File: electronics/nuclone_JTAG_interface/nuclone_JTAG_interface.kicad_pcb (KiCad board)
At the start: 2 copper layers, 50 x 50 mm, 44 parts, among them J3 nuclone_small_left, J4 nuclone_small_right

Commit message: WIP schematic
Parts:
- added J1: DevBoardUartInput, Connector_JST:JST_PH_B4B-PH-K_1x04_P2.00mm_Vertical, F.Cu at (91.3, 63.9)
- added J2: JTAG_2X10_OUT, SquantorConnectors:Header-0254-2X10-H010, F.Cu at (85.0, 107.6)
- added J5: Conn_02x05_Odd_Even, SquantorConnectors:Header-0127-2X05-H006, F.Cu at (100.3, 103.1)
- added TP36: RX, SquantorTestPoints:TestPoint_hole_H05R10_2side, F.Cu at (95.3, 68.2)
- added TP37: TX, SquantorTestPoints:TestPoint_hole_H05R10_2side, F.Cu at (97.3, 68.2)
- N2: value V20220513 -> V20230220
- moved N1 10.9 mm to (84.8, 92.8)
- moved N2 10.9 mm to (84.9, 96.5)
- moved N3 10.9 mm to (84.8, 98.0)
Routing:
- net /VBUS: track 7.40 -> 47.1 mm
- net /target_RESET: track 0.00 -> 26.2 mm, vias 0 -> 1
- net /target_TDO: track 0.00 -> 23.1 mm, vias 0 -> 1
- net /target_TCK: track 0.00 -> 17.5 mm, vias 0 -> 1
- net /target_TMS: track 0.00 -> 14.4 mm, vias 0 -> 1
- net /target_TDI: track 0.00 -> 11.8 mm, vias 0 -> 1
- net Net-(J1-Pad4): track 0.00 -> 4.30 mm
- net Net-(J1-Pad3): track 0.00 -> 4.30 mm
- net /vtarget: track 0.00 -> 2.54 mm

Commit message: WIP schematic definition
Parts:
- added C1: 1uF, SquantorRcl:C_0402, F.Cu at (85.6, 77.9)
- added C2: 1uF, SquantorRcl:C_0402, F.Cu at (88.0, 82.0)
- added C3: 1uF, SquantorRcl:C_0402, F.Cu at (88.7, 85.0)
- added C4: 1uF, SquantorRcl:C_0402, F.Cu at (83.8, 81.0)
- added C5: 1uF, SquantorRcl:C_0402, F.Cu at (85.9, 81.0)
- added C6: 1uF, SquantorRcl:C_0402, F.Cu at (81.3, 77.1)
- added C7: 1uF, SquantorRcl:C_0402, F.Cu at (83.5, 77.9)
- added F1: 0.3A, SquantorRcl:F_0603_hand, F.Cu at (81.5, 83.8)
- added Q1: NTJD4152P, SquantorIC:SOT363-ONsemi, F.Cu at (81.2, 93.6)
- added Q2: BSD840N, SquantorIC:SOT363-ONsemi, F.Cu at (75.1, 100.6)
- added R1: 10K, SquantorRcl:R_0402_hand, F.Cu at (88.7, 88.2)
- added R2: 10K, SquantorRcl:R_0402_hand, F.Cu at (83.8, 84.1)
- added R3: 4.7K, SquantorRcl:R_0402_hand, F.Cu at (81.3, 80.2)
- added R4: 10K, SquantorRcl:R_0402_hand, F.Cu at (85.9, 84.1)
- added U1: 74X1T45, SquantorIC:SOT363-NXP, F.Cu at (83.2, 100.6)
- added U2: 74X1T45, SquantorIC:SOT363-NXP, F.Cu at (93.4, 100.7)
- added U3: 74X1T45, SquantorIC:SOT363-NXP, F.Cu at (88.3, 100.7)
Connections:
- net /target_RESET renamed /PROBE_E_RST
- net /target_TCK renamed /PROBE_E_TCK
- net /target_TDI renamed /PROBE_E_TDI
- net /target_TDO renamed /PROBE_E_TDO
- net /target_TMS renamed /PROBE_E_TMS
- net /vtarget renamed /PROBE_VDD
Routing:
- net /VSS: vias 9 -> 8

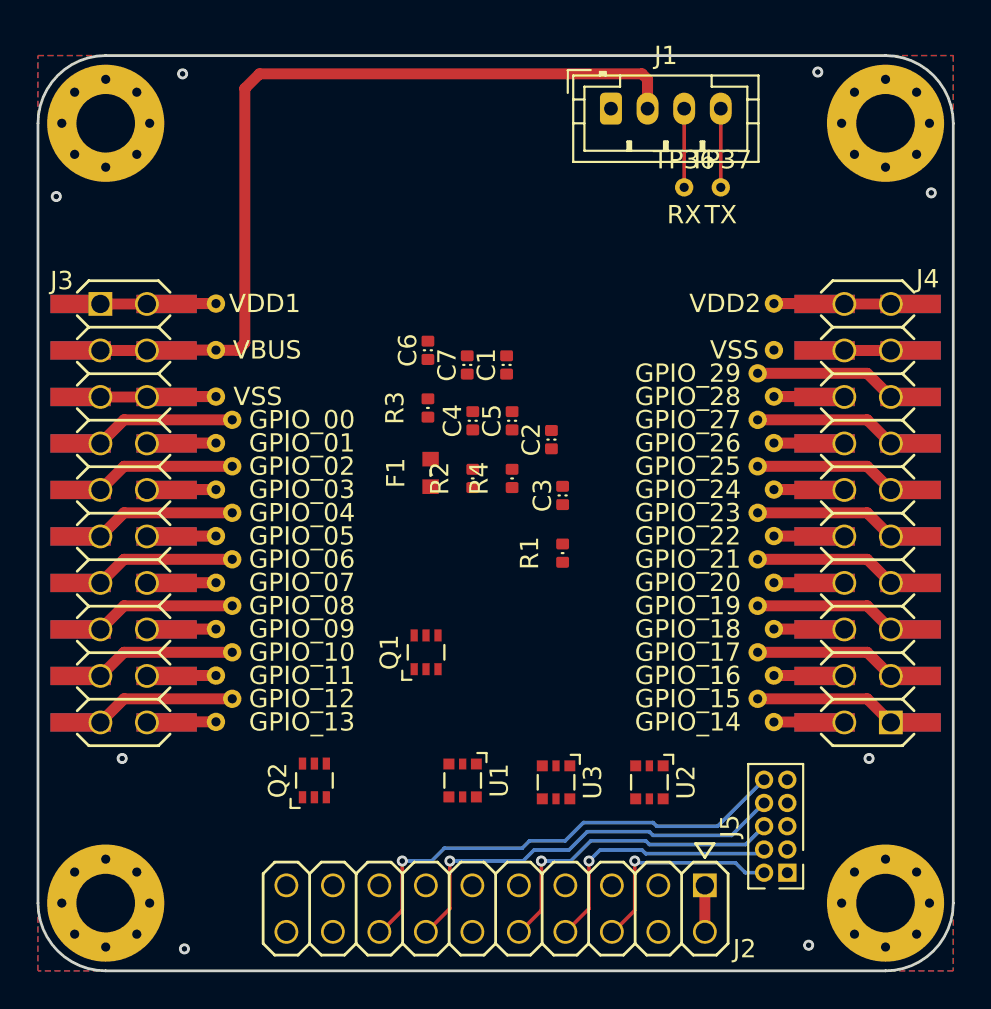
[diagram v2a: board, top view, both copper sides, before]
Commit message: added more levelshifters
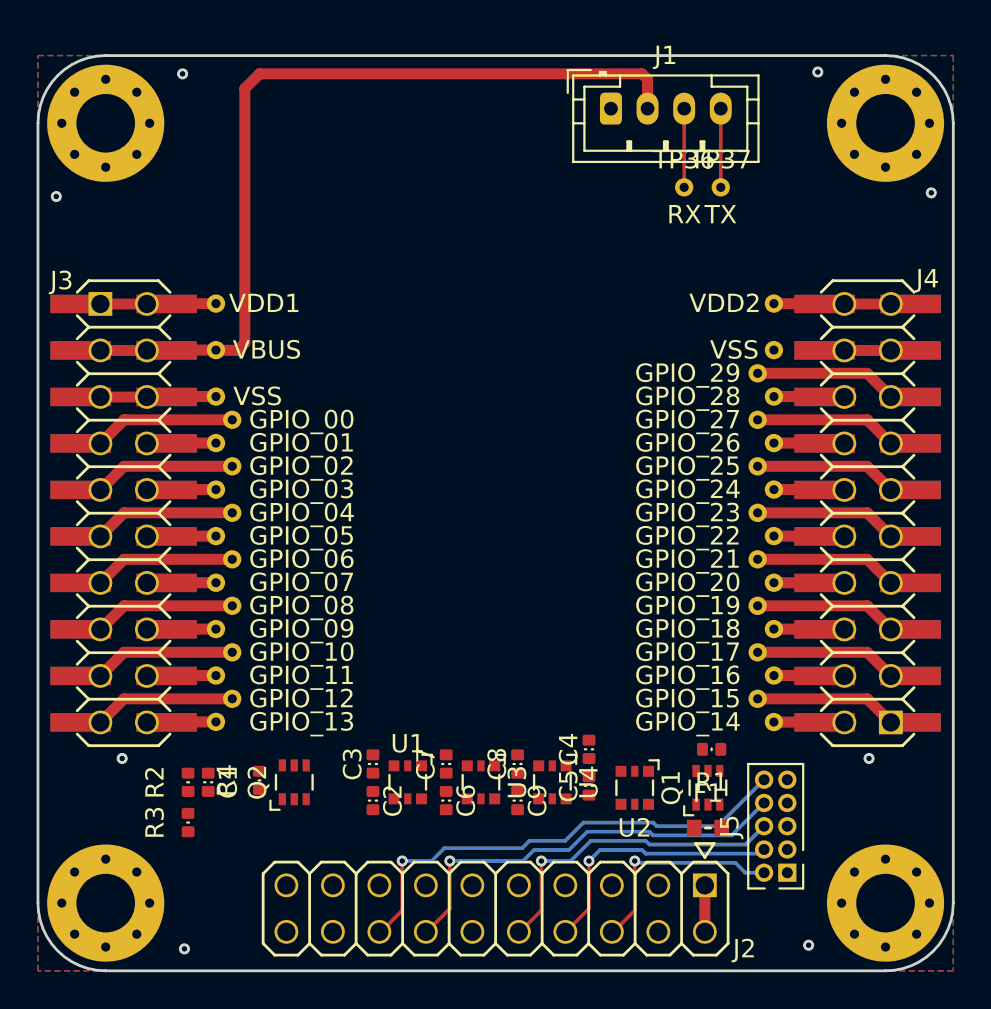
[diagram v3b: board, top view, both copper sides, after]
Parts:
- added C8: 1uF, SquantorRcl:C_0402, F.Cu at (86.2, 99.7)
- added C9: 1uF, SquantorRcl:C_0402, F.Cu at (86.2, 101.7)
- added U4: 74X1T45, SquantorIC:SOT363-NXP, F.Cu at (88.1, 100.7)
- moved C1 28.0 mm to (69.3, 100.7), turned to -90 degrees
- moved R3 26.2 mm to (68.2, 102.9)
- moved C6 24.6 mm to (82.3, 101.7), turned to -90 degrees
- moved F1 24.6 mm to (96.6, 103.2), turned to 0 degrees
- moved R2 22.7 mm to (68.2, 100.7)
- moved C2 22.0 mm to (78.3, 101.7), turned to -90 degrees
- moved C7 21.8 mm to (82.3, 99.7)
- moved R4 21.5 mm to (72.1, 100.6)
- moved C5 20.4 mm to (90.1, 100.9)
- moved C4 19.0 mm to (90.1, 98.9)
- moved C3 18.0 mm to (78.3, 99.7)
- moved Q1 17.1 mm to (96.6, 101.0)
- moved R1 13.5 mm to (96.8, 98.9), turned to 180 degrees
- moved U3 4.10 mm to (84.2, 100.7)
- moved U1 3.00 mm to (80.2, 100.7)
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
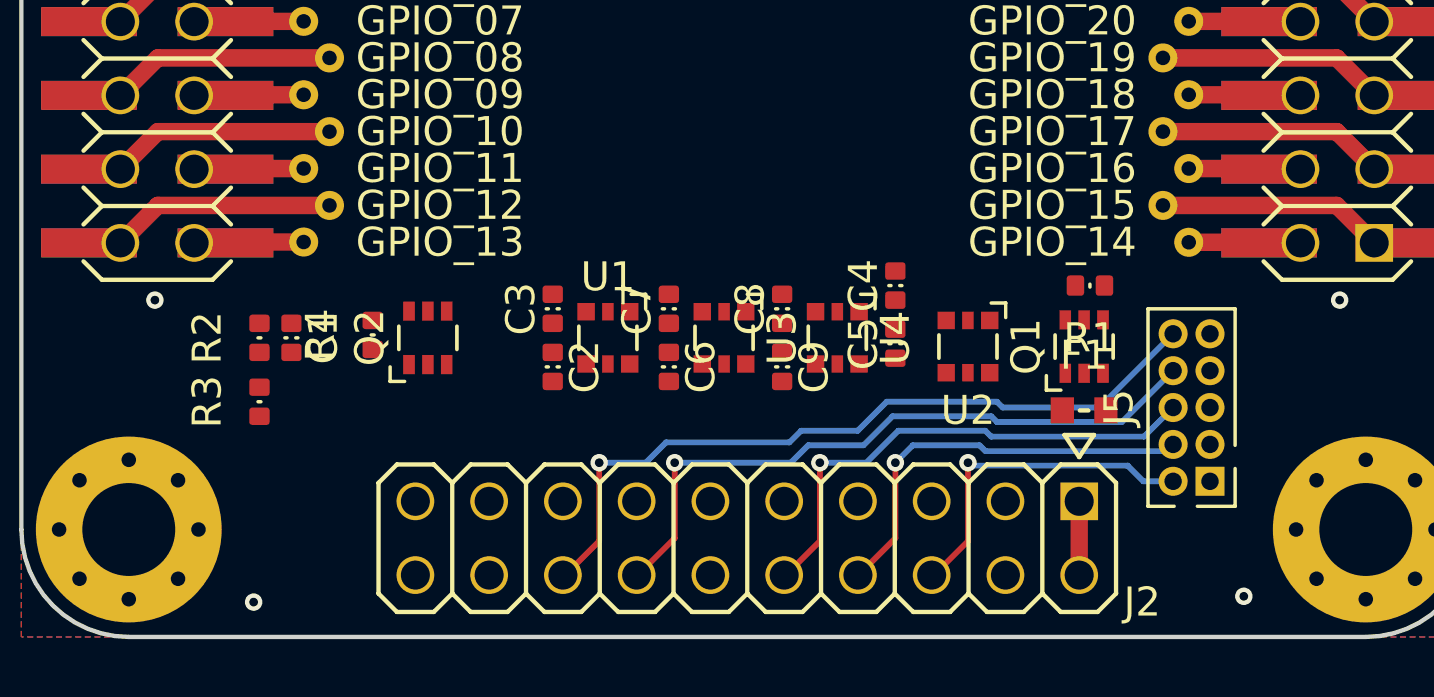
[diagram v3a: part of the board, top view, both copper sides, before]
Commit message: further routing and silk placement
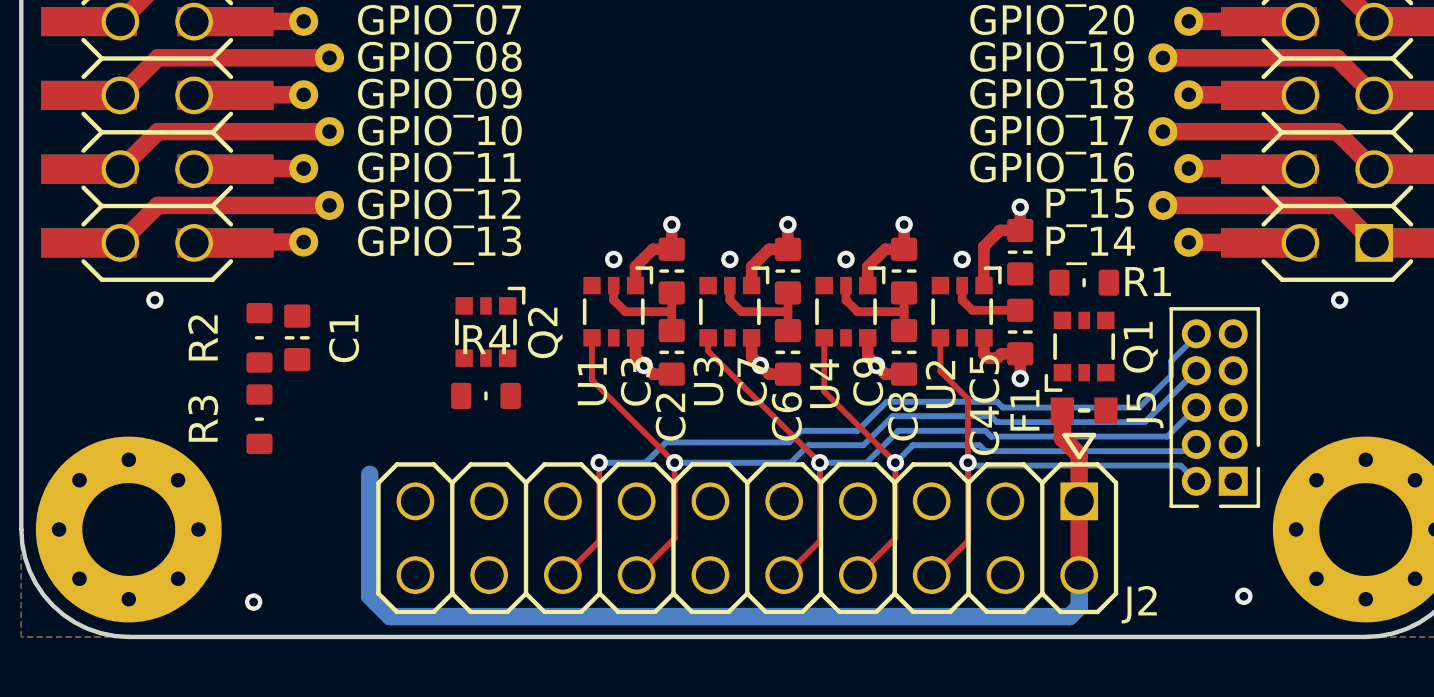
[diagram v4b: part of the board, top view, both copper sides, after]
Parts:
- C1, C2, C3, C4, C5, C6, C7, C8, C9: footprint SquantorRcl:C_0402 -> SquantorRcl:C_0603
- Q1, Q2: footprint SquantorIC:SOT363-ONsemi -> SquantorIC:SOT363-NXP
- R1, R2, R3, R4: footprint SquantorRcl:R_0402_hand -> SquantorRcl:R_0603_hand
- TP34: value GPIO_15 -> P_15
- TP35: value GPIO_14 -> P_14
- moved C9 5.34 mm to (90.4, 98.4), turned to 90 degrees
- moved C5 5.33 mm to (94.4, 97.8)
- moved C4 4.59 mm to (94.4, 100.5), turned to -90 degrees
- moved C8 4.46 mm to (90.4, 101.2), turned to -90 degrees
- moved R4 4.43 mm to (76.0, 102.7), turned to 0 degrees
- moved C3 4.30 mm to (82.4, 98.4)
- moved C7 4.30 mm to (86.4, 98.4)
- moved C2 4.13 mm to (82.4, 101.2)
- moved C6 4.13 mm to (86.4, 101.2)
- moved Q2 2.01 mm to (76.0, 100.5), turned to -90 degrees
- moved U2 1.22 mm to (92.4, 99.8)
- moved U4 0.95 mm to (88.4, 99.8)
- moved U1 0.92 mm to (80.4, 99.8)
- moved U3 0.92 mm to (84.4, 99.8)
- moved J5 0.80 mm to (101.1, 103.1)
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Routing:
- net /PROBE_VDD: track 2.54 -> 45.3 mm, vias 0 -> 4
- net /VSS: track 9.94 -> 24.5 mm, vias 8 -> 12
- net /VDD1: track 7.40 -> 20.0 mm, vias 0 -> 4
- net /PROBE_E_TCK: track 17.5 -> 24.2 mm
- net /PROBE_E_TDO: track 23.1 -> 29.4 mm
- net /PROBE_E_TMS: track 14.4 -> 20.5 mm
- net /PROBE_E_TDI: track 11.8 -> 17.3 mm
- net /PROBE_E_RST: track 26.2 -> 27.3 mm
